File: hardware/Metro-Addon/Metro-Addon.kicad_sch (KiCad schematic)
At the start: 0 parts

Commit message: feat(hw): add schematic in metro-addon
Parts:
- added BT1: Battery_Cell, Library:BAT-HLD-001, symbol Device:Battery_Cell
- added C1: 0.1uF, Capacitor_SMD:C_0805_2012Metric, symbol Device:C_Small
- added D1: Orange, LED_SMD:LED_0805_2012Metric, symbol Device:LED_Small
- added D2: Red, LED_SMD:LED_0805_2012Metric, symbol Device:LED_Small
- added D3: Blue, LED_SMD:LED_0805_2012Metric, symbol Device:LED_Small
- added D4: Green, LED_SMD:LED_0805_2012Metric, symbol Device:LED_Small
- added D5: Yellow, LED_SMD:LED_0805_2012Metric, symbol Device:LED_Small
- added J1: Conn_01x04_Socket, Connector_PinHeader_2.54mm:PinHeader_1x04_P2.54mm_Vertical, symbol Connector:Conn_01x04_Socket
- added R1, R2, R3, R4, R5: 330R, Resistor_SMD:R_0805_2012Metric, symbol Device:R_Small
- added SW1: SW_RST, Button_Switch_SMD:SW_SPST_TL3342, symbol Switch:SW_Push
- added SW2: On, Library:MSK12C02, symbol Switch:SW_DPDT_x2
- added U1: PY32F002AA15M6TU, Library:PY32F002AA15M, symbol MCU_PY32F002:PY32F002AA15M6TU
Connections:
- new net: D5.1 (K), R5.2
- new net: BT1.1 (-), SW2.2 (B)
- new net: D1.1 (K), R1.2
- new net: D4.1 (K), R4.2
- new net: D2.1 (K), R2.2
- new net: D3.1 (K), R3.2
- new net +3.3V: BT1.2 (+), C1.1, J1.2 (Pin_2), U1.1 (VCC)
- new net GND: C1.2, J1.1 (Pin_1), R1.1, R2.1, R3.1, R4.1, R5.1, SW1.1, SW2.1 (A), SW2.4 (C), U1.10 (GND)
- new net NRST: SW1.2, U1.4 (PA0/PF2-NRST)
- new net PA1: D4.2 (A), U1.5 (PA1)
- new net PA5: D3.2 (A), U1.3 (PA5/PF1-OSCOUT)
- new net PA6: D1.2 (A), U1.6 (PA6)
- new net PA7: D2.2 (A), U1.7 (PA7)
- new net PF0: D5.2 (A), U1.2 (PF0-OSCIN)
- new net SWCLK: J1.3 (Pin_3), U1.9 (PA14-SWC/PB3)
- new net SWDIO: J1.4 (Pin_4), U1.8 (PA13-SWD)
- no-connect marks 0 -> 1
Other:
- note added: "Battery"
- note added: "LED"
- note added: "Microcontroller"
- note added: "RST"

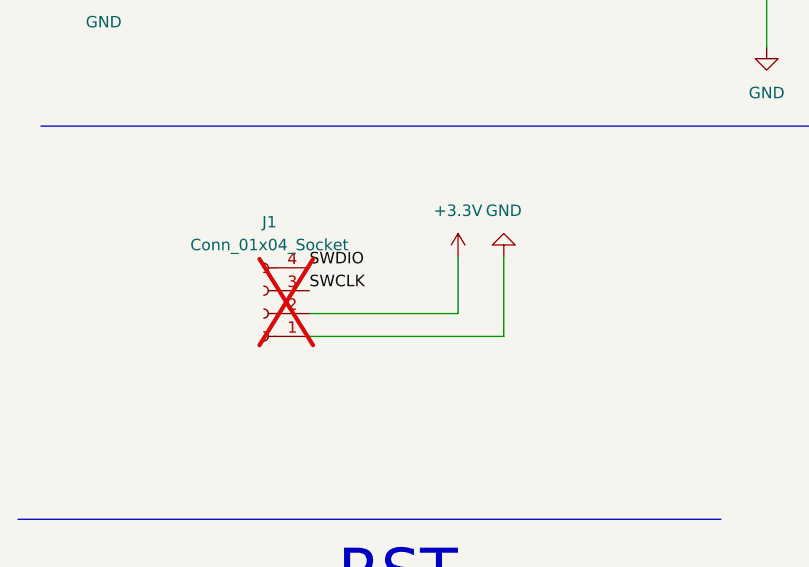
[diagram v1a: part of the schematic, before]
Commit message: feat(hw): add routes in metro addon
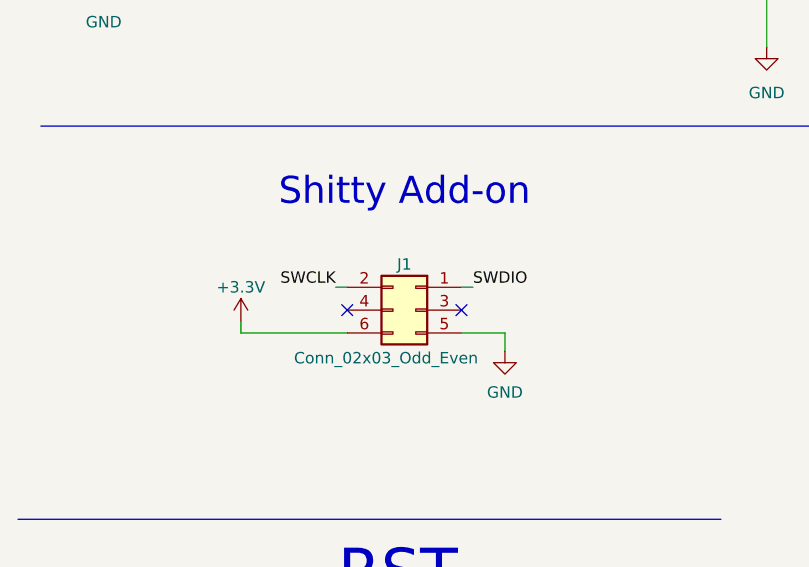
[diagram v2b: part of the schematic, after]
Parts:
- removed J1: Conn_01x04_Socket, Connector_PinHeader_2.54mm:PinHeader_1x04_P2.54mm_Vertical, symbol Connector:Conn_01x04_Socket
- added J1: Conn_02x03_Odd_Even, Library:B-2100N06P-B111_CKM, symbol Connector_Generic:Conn_02x03_Odd_Even
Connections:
- net +3.3V: now also J1.6 (Pin_6)
- net GND: now also J1.5 (Pin_5)
- net SWCLK: now also J1.2 (Pin_2)
- net SWDIO: now also J1.1 (Pin_1)
- no-connect marks 1 -> 3
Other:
- note added: "Shitty Add-on"

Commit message: feat(Hw):Labels-Added
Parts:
- J1: LCSC# C124390 -> C780054
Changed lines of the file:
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@@
 			)
 		)
-		(property "LCSC#" "C124390"
+		(property "LCSC#" "C780054"
 			(at 56.261 82.55 0)
 			(effects

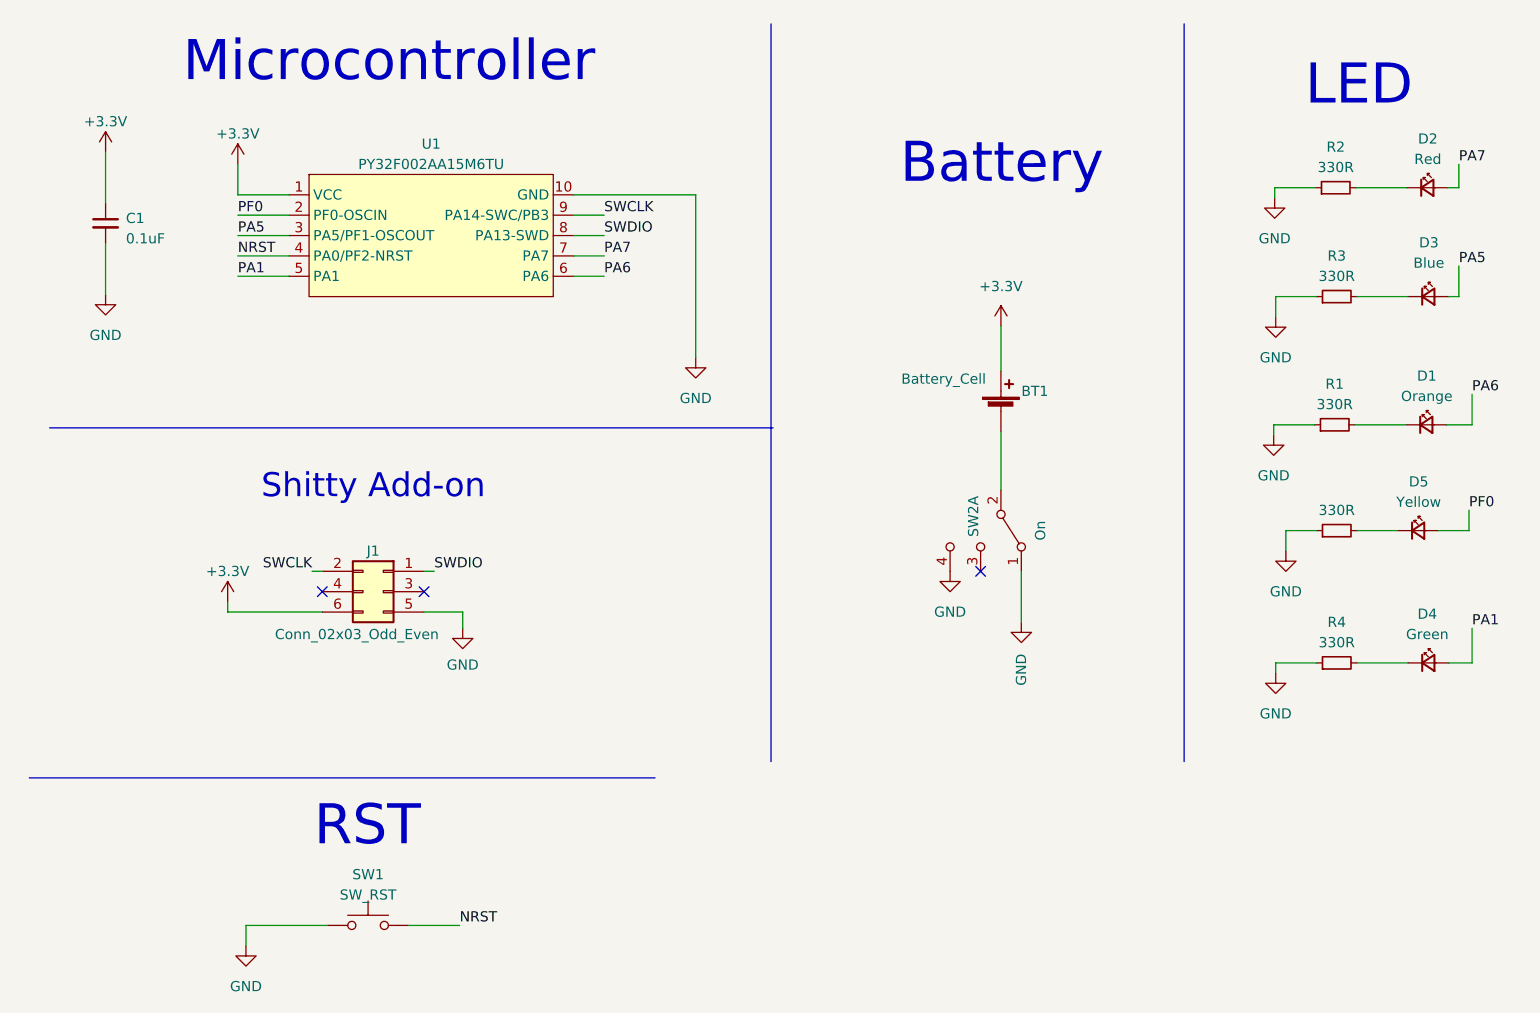
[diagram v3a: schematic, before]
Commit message: feat(Hw):Led_Modified
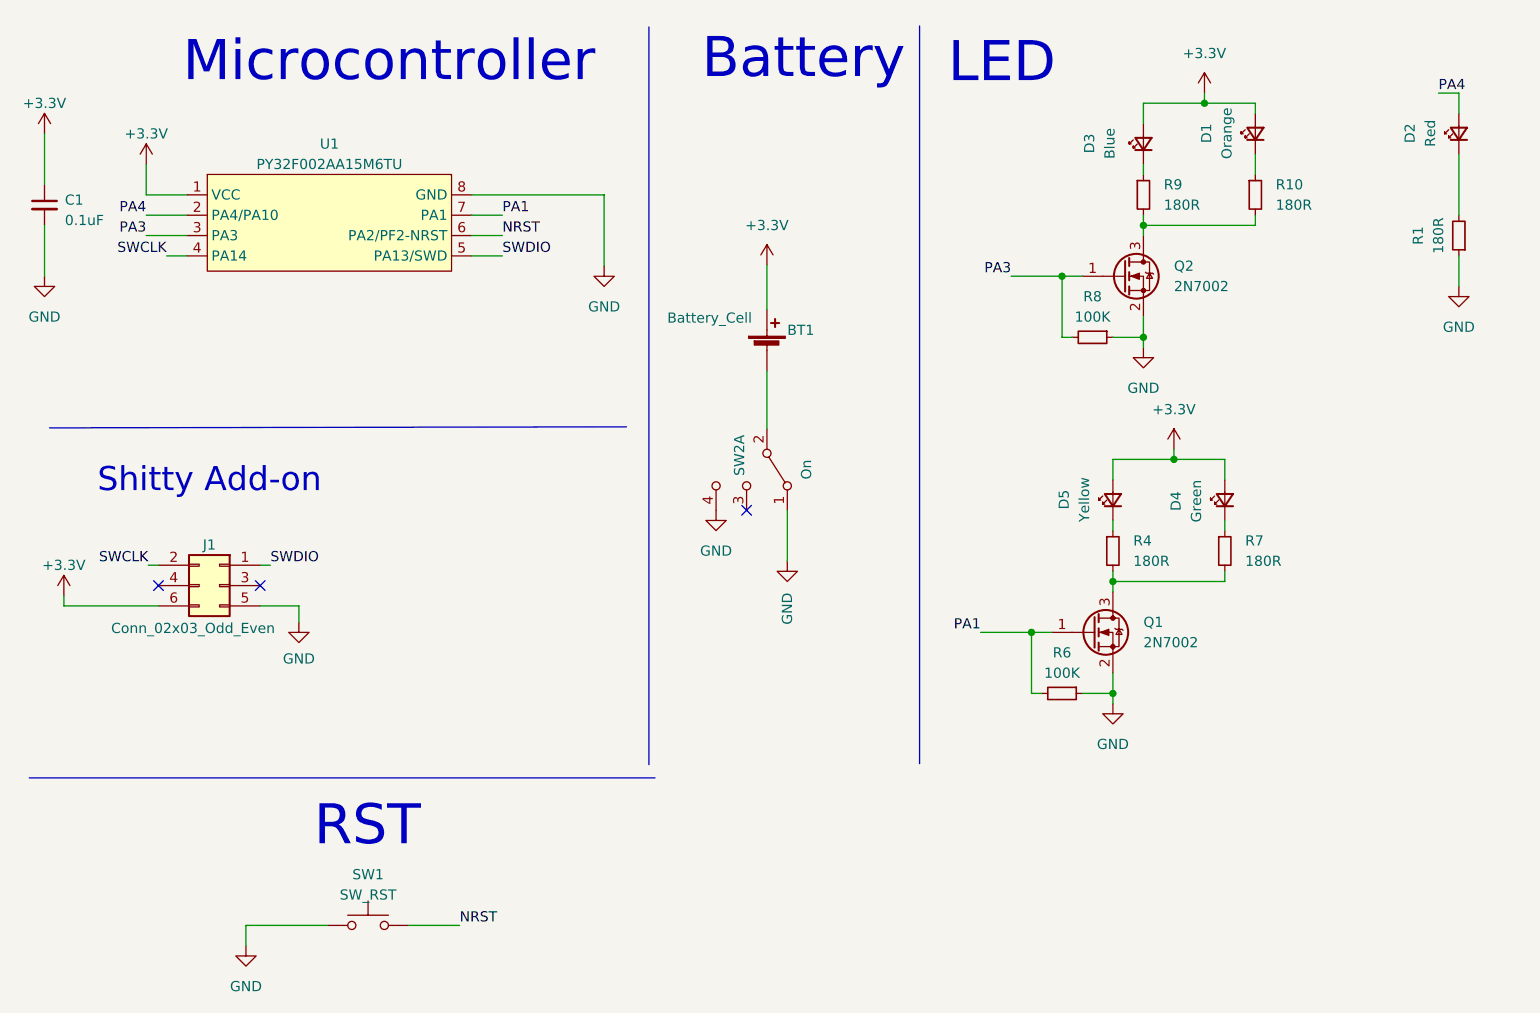
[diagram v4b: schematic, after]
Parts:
- removed R2, R3, R5: 330R, Resistor_SMD:R_0805_2012Metric, symbol Device:R_Small
- added Q1, Q2: 2N7002, Package_TO_SOT_SMD:SOT-23, symbol Transistor_FET:2N7002
- added R10, R7, R9: 180R, Resistor_SMD:R_0805_2012Metric, symbol Device:R_Small
- added R6, R8: 100K, Resistor_SMD:R_0805_2012Metric, symbol Device:R_Small
- R1, R4: value 330R -> 180R; LCSC# C119075 -> C1339
- U1: footprint Library:PY32F002AA15M -> Library:PY32F002AL15S6TU; LCSC# C5292058 -> C5292060
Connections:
- net +3.3V: now also D1.2 (A), D3.2 (A), D4.2 (A), D5.2 (A)
- net GND: now also U1.8 (GND), Q1.2 (S), Q2.2 (S), R6.1, R8.1; no longer R4.1, U1.10 (GND)
- net NRST: now also U1.6 (PA2/PF2-NRST); no longer U1.4 (PA0/PF2-NRST)
- net PA1: now also U1.7 (PA1), Q1.1 (G), R6.2; no longer D4.2 (A), U1.5 (PA1)
- net SWCLK: now also U1.4 (PA14); no longer U1.9 (PA14-SWC/PB3)
- net SWDIO: now also U1.5 (PA13/SWD); no longer U1.8 (PA13-SWD)
- net at D5.1 (K): now also R4.1
- net at R1.2: now also D2.1 (K); no longer D1.1 (K)
- net at D4.1 (K): now also R7.1; no longer R4.2
- net at D3.1 (K): now also R9.1
- net PA5 renamed PA3
- net PA3: now also Q2.1 (G), R8.2; no longer D3.2 (A)
- removed net PA6: D1.2 (A), U1.6 (PA6)
- net PA7 renamed PA4
- net PA4: now also U1.2 (PA4/PA10); no longer U1.7 (PA7)
- removed net PF0: D5.2 (A), U1.2 (PF0-OSCIN)
- new net: Q1.3 (D), R4.2, R7.2
- new net: Q2.3 (D), R10.2, R9.2
- new net: D1.1 (K), R10.1
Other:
- moved on the sheet: BT1, C1, D1, D2, D3, D4, D5, J1, R4, SW2A

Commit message: feat(Hw):Update_BOM
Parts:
- Q1, Q2: LCSC# (none) -> C8545
- R6, R8: LCSC# C119075 -> C96346
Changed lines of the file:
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@@
+			)
+		)
+		(property "LCSC#" "C8545"
+			(at 144.78 87.63 0)
+			(effects
+				(font
+					(size 1.27 1.27)
+				)
+				(hide yes)
 			)
 		)
@@
 			)
 		)
+		(property "LCSC#" "C8545"
+			(at 148.59 43.18 0)
+			(effects
+				(font
+					(size 1.27 1.27)
+				)
+				(hide yes)
+			)
+		)
 		(pin "2"
 		)
@@
 			)
 		)
-		(property "LCSC#" "C119075"
+		(property "LCSC#" "C96346"
 			(at 144.78 50.8 0)
 			(effects
@@
 			)
 		)
-		(property "LCSC#" "C119075"
+		(property "LCSC#" "C96346"
 			(at 140.97 95.25 0)
 			(effects

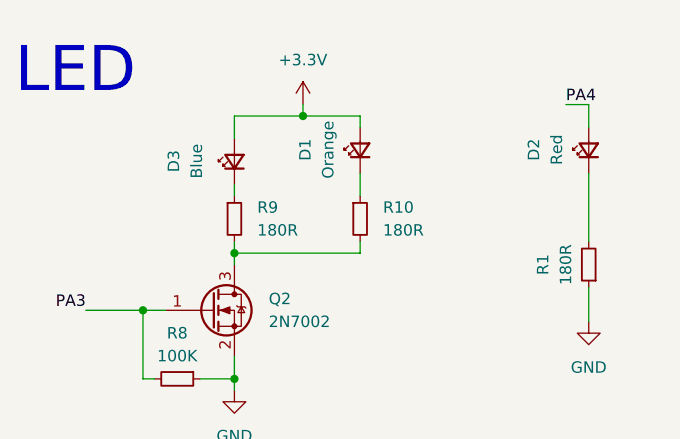
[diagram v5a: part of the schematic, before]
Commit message: feat(Hw):Mounting_Hole_Added
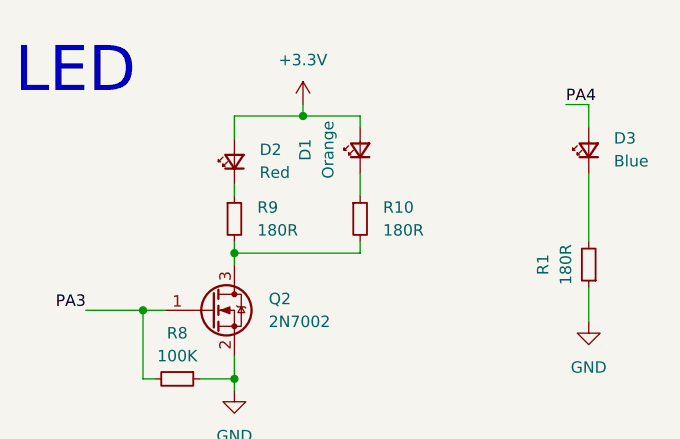
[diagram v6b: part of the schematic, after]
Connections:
- net +3.3V: now also D2.2 (A); no longer D3.2 (A)
- net PA4: now also D3.2 (A); no longer D2.2 (A)
- net at R1.2: now also D3.1 (K); no longer D2.1 (K)
- net at R9.1: now also D2.1 (K); no longer D3.1 (K)
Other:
- moved on the sheet: D2, D3
